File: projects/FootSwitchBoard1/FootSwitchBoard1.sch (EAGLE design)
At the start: 46 parts

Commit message: Work in progress, switching back to reverse polarity protection only.
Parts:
- DDUB1, DDUB2: value 1N58172 -> (none); device gm-diodes:1N58172 -> gm-diodes:1N47XX3
- DZ: device gm-diodes:1N47XX2 -> gm-diodes:1N47XX3
- R1, R2, R5: device gm-resistors:6MM.2 -> gm-resistors:6MM.3
- TC1044S: device ic-package:DIL8S -> gm-ics:DIL8
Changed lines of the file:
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@@
 <part name="G4" library="wirepad" deviceset="WIREPAD" device="2,15/1,0" value="WIREPAD2,15/1,0"/>
 <part name="G5" library="wirepad" deviceset="WIREPAD" device="2,15/1,0" value="WIREPAD2,15/1,0"/>
-<part name="TC1044S" library="ic-package" deviceset="DIL8" device="S"/>
-<part name="DDUB1" library="gm-diodes" deviceset="1N5817" device="2"/>
-<part name="DDUB2" library="gm-diodes" deviceset="1N5817" device="2"/>
+<part name="TC1044S" library="gm-ics" deviceset="DIL8" device=""/>
+<part name="DDUB1" library="gm-diodes" deviceset="1N47XX" device="3"/>
+<part name="DDUB2" library="gm-diodes" deviceset="1N47XX" device="3"/>
 <part name="CDUB1" library="gm-caps-electro-pol" deviceset="050" device="" value="10u"/>
 <part name="CDUB2" library="gm-caps-electro-pol" deviceset="050" device="" value="10u"/>
@@
 <part name="PNP1" library="gm-trans" deviceset="2N3906" device="-" value="2N3906-"/>
 <part name="PNP2" library="gm-trans" deviceset="2N3906" device="-" value="2N3906-"/>
-<part name="R1" library="gm-resistors" deviceset="6MM" device=".2" value="10k"/>
-<part name="R2" library="gm-resistors" deviceset="6MM" device=".2" value="10k"/>
-<part name="R5" library="gm-resistors" deviceset="6MM" device=".2" value="100k"/>
-<part name="DZ" library="gm-diodes" deviceset="1N47XX" device="2"/>
+<part name="R1" library="gm-resistors" deviceset="6MM" device=".3" value="10k"/>
+<part name="R2" library="gm-resistors" deviceset="6MM" device=".3" value="10k"/>
+<part name="R5" library="gm-resistors" deviceset="6MM" device=".3" value="100k"/>
+<part name="DZ" library="gm-diodes" deviceset="1N47XX" device="3"/>
 </parts>
 <sheets>
@@
 <instance part="G5" gate="G$1" x="5.08" y="7.62"/>
 <instance part="TC1044S" gate="G$1" x="162.56" y="53.34"/>
-<instance part="DDUB1" gate="G$1" x="182.88" y="55.88"/>
-<instance part="DDUB2" gate="G$1" x="205.74" y="43.18"/>
+<instance part="DDUB1" gate="1" x="182.88" y="55.88"/>
+<instance part="DDUB2" gate="1" x="205.74" y="43.18"/>
 <instance part="CDUB1" gate="1" x="193.04" y="40.64"/>
 <instance part="CDUB2" gate="1" x="210.82" y="40.64"/>
@@
 <segment>
 <pinref part="TC1044S" gate="G$1" pin="8"/>
-<pinref part="DDUB1" gate="G$1" pin="A"/>
+<pinref part="DDUB1" gate="1" pin="A"/>
 <wire x1="180.34" y1="55.88" x2="170.18" y2="55.88" width="0.1524" layer="91"/>
 <wire x1="180.34" y1="55.88" x2="177.8" y2="60.96" width="0.1524" layer="91"/>
@@
 <net name="DDUB2" class="0">
 <segment>
-<pinref part="DDUB1" gate="G$1" pin="C"/>
+<pinref part="DDUB1" gate="1" pin="C"/>
 <pinref part="CDUB1" gate="1" pin="+"/>
 <wire x1="187.96" y1="55.88" x2="193.04" y2="55.88" width="0.1524" layer="91"/>
 <wire x1="193.04" y1="55.88" x2="193.04" y2="43.18" width="0.1524" layer="91"/>
-<pinref part="DDUB2" gate="G$1" pin="A"/>
+<pinref part="DDUB2" gate="1" pin="A"/>
 <wire x1="193.04" y1="43.18" x2="203.2" y2="43.18" width="0.1524" layer="91"/>
 <junction x="193.04" y="43.18"/>
@@
 <net name="N$22" class="0">
 <segment>
-<pinref part="DDUB2" gate="G$1" pin="C"/>
+<pinref part="DDUB2" gate="1" pin="C"/>
 <pinref part="CDUB2" gate="1" pin="+"/>
 <pinref part="18" gate="G$1" pin="P"/>

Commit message: Good layout with reverse polarity protection.
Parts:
- removed BDO1: WIREPAD2,15/1,0, wirepad:WIREPAD2,15/1,0
- removed DZ: (no value), gm-diodes:1N47XX3
- removed PNP2: 2N3906-, gm-trans:2N3906-
- added D1: 1N4148-3, gm-diodes:1N4148-3
- added NPN1: 2N3904, gm-trans:2N3904
- added R6: 4M7, gm-resistors:6MM.3
- R1: value 10k -> 100K
- R2: value 10k -> 3K3
- R5: value 100k -> 10K
- RIN, ROUT: device gm-resistors:6MM.3 -> gm-resistors:6MM.2
- renumbered C1 to CIN1, C2 to CIN2, C3 to CV/2, R3 to RV/2A, R4 to RV/2B
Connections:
- removed net N$23: PNP1.B, PNP2.C, R1.2
- removed net N$3: BDO.P, BDO1.P, U$1.C3
- removed net N$4: BDI.P, U$1.B2
- new net N$11: BDO.P, ROUT.2, U$1.C3
- new net N$7: PNP1.B, R2.2, R6.1
- new net N$8: BDI.P, RIN.2, U$1.B2
- net GDUBINV: now also D1.A, NPN1.E; no longer DZ.A
- net N$1: no longer RIN.2
- net N$14: now also D1.C, NPN1.B, R1.2; no longer DZ.C, R2.1
- net N$2: no longer ROUT.2
- net N$24: now also R6.2; no longer PNP2.E
- net N$9: now also NPN1.C, R2.1; no longer PNP2.B, R2.2
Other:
- moved on the sheet: PNP1, R1, R2, R5

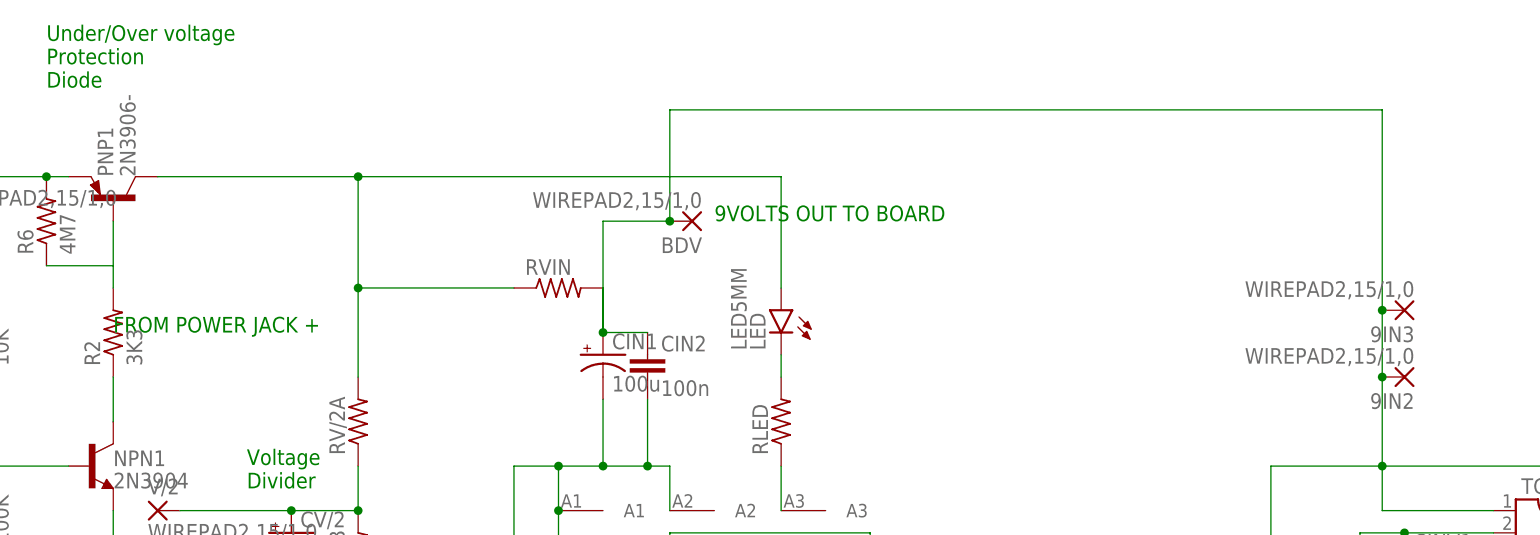
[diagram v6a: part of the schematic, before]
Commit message: Finalized layout with ground and power planes.
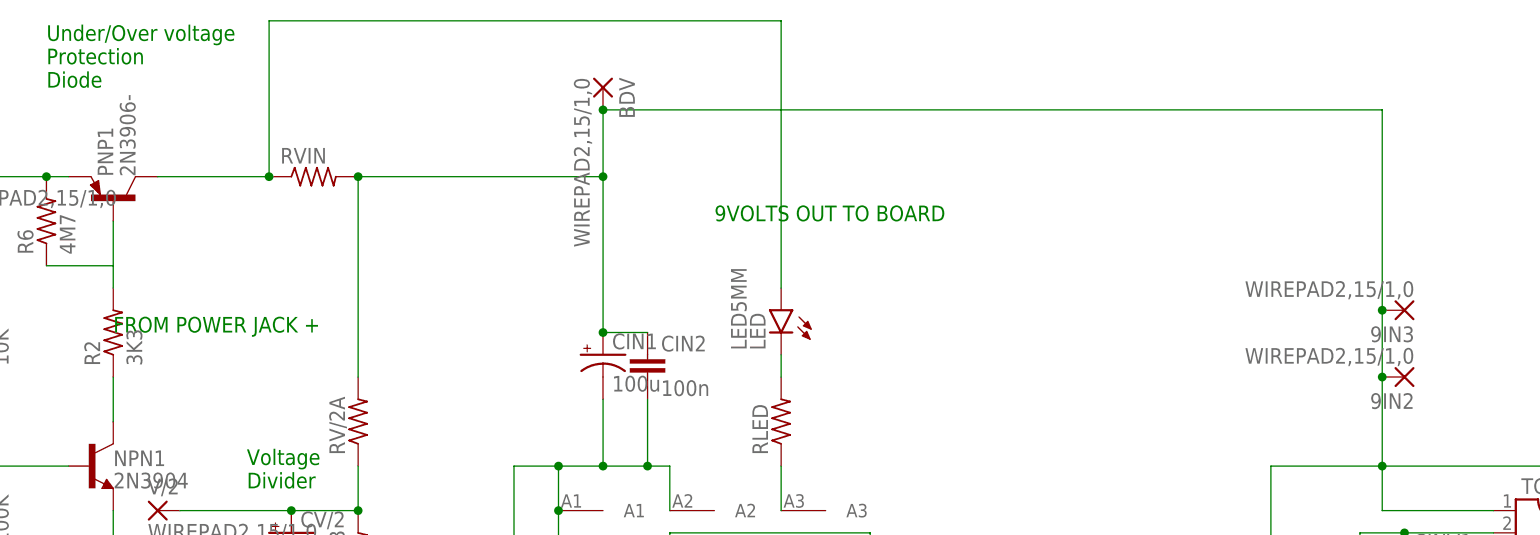
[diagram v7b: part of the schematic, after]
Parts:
- CDUB1, CDUB2, CINV1, CINV2: device gm-caps-electro-pol:050 -> gm-caps-electro-pol:0501
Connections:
- removed net N$25: LED.A, PNP1.C, RV/2A.2, RVIN.1
- new net N$4: LED.A, PNP1.C, RVIN.1
- net 9INDUBINV: now also RV/2A.2
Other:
- moved on the sheet: BDV, RVIN
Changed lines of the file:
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@@
 <part name="DDUB1" library="gm-diodes" deviceset="1N47XX" device="3"/>
 <part name="DDUB2" library="gm-diodes" deviceset="1N47XX" device="3"/>
-<part name="CDUB1" library="gm-caps-electro-pol" deviceset="050" device="" value="10u"/>
-<part name="CDUB2" library="gm-caps-electro-pol" deviceset="050" device="" value="10u"/>
+<part name="CDUB1" library="gm-caps-electro-pol" deviceset="050" device="1" value="10u"/>
+<part name="CDUB2" library="gm-caps-electro-pol" deviceset="050" device="1" value="10u"/>
 <part name="G8" library="wirepad" deviceset="WIREPAD" device="2,15/1,0" value="WIREPAD2,15/1,0"/>
 <part name="9IN2" library="wirepad" deviceset="WIREPAD" device="2,15/1,0" value="WIREPAD2,15/1,0"/>
 <part name="18" library="wirepad" deviceset="WIREPAD" device="2,15/1,0" value="WIREPAD2,15/1,0"/>
 <part name="G6" library="wirepad" deviceset="WIREPAD" device="2,15/1,0" value="WIREPAD2,15/1,0"/>
-<part name="RIN" library="gm-resistors" deviceset="6MM" device=".2"/>
 <part name="ROUT" library="gm-resistors" deviceset="6MM" device=".2"/>
-<part name="CINV1" library="gm-caps-electro-pol" deviceset="050" device="" value="10u"/>
-<part name="CINV2" library="gm-caps-electro-pol" deviceset="050" device="" value="10u"/>
+<part name="CINV1" library="gm-caps-electro-pol" deviceset="050" device="1" value="10u"/>
+<part name="CINV2" library="gm-caps-electro-pol" deviceset="050" device="1" value="10u"/>
 <part name="9IN3" library="wirepad" deviceset="WIREPAD" device="2,15/1,0" value="WIREPAD2,15/1,0"/>
 <part name="G9" library="wirepad" deviceset="WIREPAD" device="2,15/1,0" value="WIREPAD2,15/1,0"/>
@@
 <part name="R6" library="gm-resistors" deviceset="6MM" device=".3" value="4M7"/>
 <part name="D1" library="gm-diodes" deviceset="1N4148" device="-3"/>
+<part name="RIN" library="gm-resistors" deviceset="6MM" device=".2"/>
 </parts>
 <sheets>
@@
 <instance part="LED" gate="G$1" x="73.66" y="76.2" rot="MR90"/>
 <instance part="RLED" gate="G$1" x="73.66" y="66.04" rot="R90"/>
-<instance part="RVIN" gate="G$1" x="48.26" y="81.28"/>
+<instance part="RVIN" gate="G$1" x="20.32" y="93.98"/>
 <instance part="CIN1" gate="G$1" x="53.34" y="73.66"/>
 <instance part="CIN2" gate="G$1" x="58.42" y="71.12"/>
@@
 <instance part="G0" gate="G$1" x="5.08" y="45.72"/>
 <instance part="V/2" gate="G$1" x="2.54" y="55.88"/>
-<instance part="BDV" gate="G$1" x="63.5" y="88.9" rot="R180"/>
+<instance part="BDV" gate="G$1" x="53.34" y="104.14" rot="R270"/>
 <instance part="G1" gate="G$1" x="5.08" y="38.1"/>
 <instance part="G2" gate="G$1" x="5.08" y="30.48"/>
@@
 <instance part="18" gate="G$1" x="215.9" y="53.34" rot="R180"/>
 <instance part="G6" gate="G$1" x="5.08" y="-2.54"/>
-<instance part="RIN" gate="G$1" x="30.48" y="27.94"/>
 <instance part="ROUT" gate="G$1" x="30.48" y="17.78"/>
 <instance part="CINV1" gate="1" x="144.78" y="50.8"/>
@@
 <instance part="R6" gate="G$1" x="-10.16" y="88.9" rot="R90"/>
 <instance part="D1" gate="G$1" x="-22.86" y="55.88" rot="R90"/>
+<instance part="RIN" gate="G$1" x="30.48" y="27.94"/>
 </instances>
 <busses>
@@
 <wire x1="25.4" y1="17.78" x2="22.86" y2="17.78" width="0.1524" layer="91"/>
 <junction x="22.86" y="17.78"/>
-<pinref part="RIN" gate="G$1" pin="1"/>
 <wire x1="25.4" y1="27.94" x2="22.86" y2="27.94" width="0.1524" layer="91"/>
 <junction x="22.86" y="27.94"/>
@@
 <wire x1="-2.54" y1="55.88" x2="-2.54" y2="50.8" width="0.1524" layer="91"/>
 <junction x="-2.54" y="50.8"/>
+<pinref part="RIN" gate="G$1" pin="1"/>
 </segment>
 </net>
@@
 <wire x1="129.54" y1="50.8" x2="129.54" y2="60.96" width="0.1524" layer="91"/>
 <wire x1="129.54" y1="60.96" x2="142.24" y2="60.96" width="0.1524" layer="91"/>
-<pinref part="CIN1" gate="G$1" pin="+"/>
-<pinref part="CIN2" gate="G$1" pin="1"/>
-<wire x1="53.34" y1="76.2" x2="58.42" y2="76.2" width="0.1524" layer="91"/>
-<pinref part="RVIN" gate="G$1" pin="2"/>
-<junction x="53.34" y="76.2"/>
 <pinref part="BDV" gate="G$1" pin="P"/>
-<wire x1="60.96" y1="88.9" x2="53.34" y2="88.9" width="0.1524" layer="91"/>
-<wire x1="53.34" y1="88.9" x2="53.34" y2="76.2" width="0.1524" layer="91"/>
-<wire x1="53.34" y1="76.2" x2="53.34" y2="81.28" width="0.1524" layer="91"/>
-<wire x1="60.96" y1="88.9" x2="60.96" y2="101.6" width="0.1524" layer="91"/>
-<junction x="60.96" y="88.9"/>
-<wire x1="60.96" y1="101.6" x2="142.24" y2="101.6" width="0.1524" layer="91"/>
+<wire x1="53.34" y1="101.6" x2="142.24" y2="101.6" width="0.1524" layer="91"/>
 <wire x1="142.24" y1="101.6" x2="142.24" y2="78.74" width="0.1524" layer="91"/>
 <junction x="142.24" y="78.74"/>
+<wire x1="53.34" y1="93.98" x2="25.4" y2="93.98" width="0.1524" layer="91"/>
+<wire x1="25.4" y1="93.98" x2="25.4" y2="71.12" width="0.1524" layer="91"/>
+<pinref part="RV/2A" gate="G$1" pin="2"/>
+<pinref part="RVIN" gate="G$1" pin="2"/>
+<junction x="25.4" y="93.98"/>
+<wire x1="53.34" y1="101.6" x2="53.34" y2="93.98" width="0.1524" layer="91"/>
+<junction x="53.34" y="101.6"/>
+<junction x="53.34" y="93.98"/>
+<pinref part="CIN2" gate="G$1" pin="1"/>
+<pinref part="CIN1" gate="G$1" pin="+"/>
+<wire x1="53.34" y1="76.2" x2="58.42" y2="76.2" width="0.1524" layer="91"/>
+<wire x1="53.34" y1="76.2" x2="53.34" y2="93.98" width="0.1524" layer="91"/>
+<junction x="53.34" y="76.2"/>
 </segment>
 </net>
@@
 </segment>
 </net>
-<net name="N$25" class="0">
-<segment>
-<pinref part="RVIN" gate="G$1" pin="1"/>
-<pinref part="LED" gate="G$1" pin="A"/>
-<wire x1="73.66" y1="81.28" x2="73.66" y2="93.98" width="0.1524" layer="91"/>
-<wire x1="73.66" y1="93.98" x2="25.4" y2="93.98" width="0.1524" layer="91"/>
-<wire x1="25.4" y1="93.98" x2="25.4" y2="81.28" width="0.1524" layer="91"/>
-<junction x="25.4" y="81.28"/>
-<wire x1="25.4" y1="81.28" x2="43.18" y2="81.28" width="0.1524" layer="91"/>
-<pinref part="RV/2A" gate="G$1" pin="2"/>
-<wire x1="25.4" y1="71.12" x2="25.4" y2="81.28" width="0.1524" layer="91"/>
-<pinref part="PNP1" gate="G$1" pin="C"/>
-<wire x1="2.54" y1="93.98" x2="25.4" y2="93.98" width="0.1524" layer="91"/>
-<junction x="25.4" y="93.98"/>
-</segment>
-</net>
 <net name="N$7" class="0">
 <segment>
@@
 <net name="N$8" class="0">
 <segment>
-<pinref part="RIN" gate="G$1" pin="2"/>
 <pinref part="U$1" gate="G$1" pin="B2"/>
 <wire x1="60.96" y1="50.8" x2="60.96" y2="53.34" width="0.1524" layer="91"/>
@@
 <wire x1="83.82" y1="27.94" x2="83.82" y2="33.02" width="0.1524" layer="91"/>
 <junction x="83.82" y="33.02"/>
+<pinref part="RIN" gate="G$1" pin="2"/>
 </segment>
 </net>
@@
 </segment>
 </net>
+<net name="N$4" class="0">
+<segment>
+<pinref part="LED" gate="G$1" pin="A"/>
+<wire x1="73.66" y1="81.28" x2="73.66" y2="111.76" width="0.1524" layer="91"/>
+<pinref part="PNP1" gate="G$1" pin="C"/>
+<pinref part="RVIN" gate="G$1" pin="1"/>
+<wire x1="15.24" y1="93.98" x2="2.54" y2="93.98" width="0.1524" layer="91"/>
+<wire x1="73.66" y1="111.76" x2="15.24" y2="111.76" width="0.1524" layer="91"/>
+<wire x1="15.24" y1="111.76" x2="15.24" y2="93.98" width="0.1524" layer="91"/>
+<junction x="15.24" y="93.98"/>
+</segment>
+</net>

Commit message: Final version of files.
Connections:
- net GDUBINV: now also TC1044S.3
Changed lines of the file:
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@@
-</segment>
-</net>
-<net name="-9GND" class="0">
-<segment>
-<wire x1="198.12" y1="-12.7" x2="198.12" y2="-15.24" width="0.1524" layer="91"/>
 </segment>
 </net>
@@
 <junction x="-2.54" y="50.8"/>
 <pinref part="RIN" gate="G$1" pin="1"/>
+<pinref part="TC1044S" gate="G$1" pin="3"/>
+<wire x1="154.94" y1="50.8" x2="149.86" y2="50.8" width="0.1524" layer="91"/>
+<wire x1="149.86" y1="50.8" x2="149.86" y2="33.02" width="0.1524" layer="91"/>
 </segment>
 </net>
@@
 <pinref part="R2" gate="G$1" pin="2"/>
 <pinref part="R6" gate="G$1" pin="1"/>
-<wire x1="-10.16" y1="83.82" x2="-2.54" y2="83.82" width="0.1524" layer="91"/>
+<wire x1="-10.16" y1="83.82" x2="-7.62" y2="83.82" width="0.1524" layer="91"/>
 <wire x1="-2.54" y1="83.82" x2="-2.54" y2="88.9" width="0.1524" layer="91"/>
 <wire x1="-2.54" y1="83.82" x2="-2.54" y2="81.28" width="0.1524" layer="91"/>
-</segment>
-</net>
+<wire x1="-7.62" y1="83.82" x2="-2.54" y2="83.82" width="0.1524" layer="91"/>
+<junction x="-2.54" y="83.82"/>
+</segment>
+</net>
